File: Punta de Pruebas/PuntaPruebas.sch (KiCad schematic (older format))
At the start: 23 parts, among them P1 CONN_2, P2 CONN_1, P3 CONN_1, SW1 Llave Inversora, U1 40106

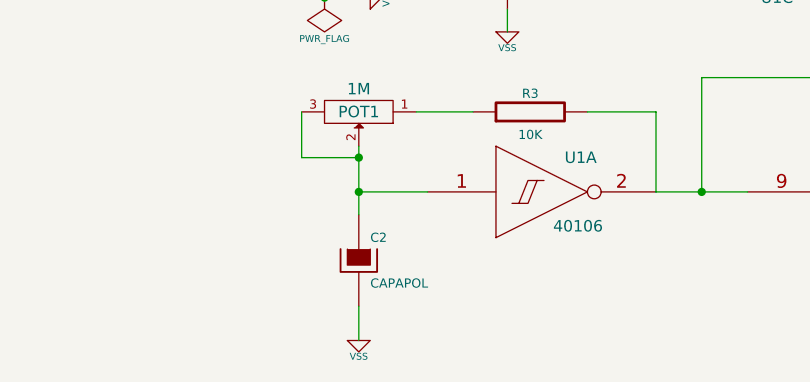
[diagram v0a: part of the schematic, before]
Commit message: Realizo un layout alternativo del PCB, haciendo más claro el ensamblado
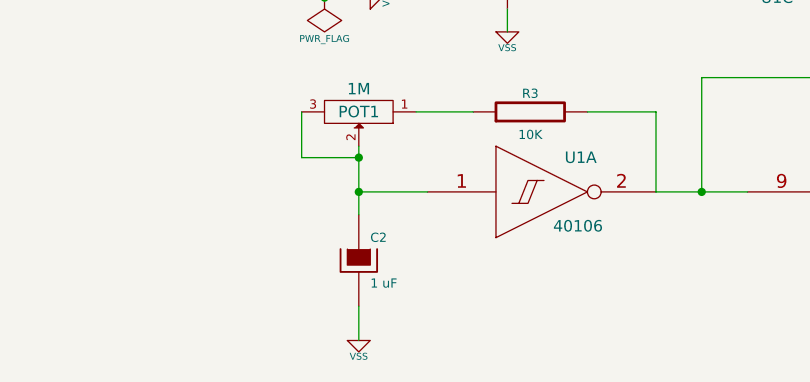
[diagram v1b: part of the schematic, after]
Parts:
- C2: value CAPAPOL -> 1 uF
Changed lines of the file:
@@
 LIBS:contrib
 LIBS:valves
-LIBS:w_device
 LIBS:PuntaPruebas-cache
-EELAYER 27 0
+EELAYER 24 0
 EELAYER END
 $Descr A4 11693 8268
@@
 Rev "1.0"
 Comp "Nestor A. Scoccia"
-Comment1 ""
+Comment1 "Proyecto N° 3"
 Comment2 ""
 Comment3 ""
@@
 P 3650 4950
 F 0 "C2" H 3700 5050 40  0000 L CNN
-F 1 "CAPAPOL" H 3700 4850 40  0000 L CNN
+F 1 "1 uF" H 3700 4850 40  0000 L CNN
 F 2 "~" H 3750 4800 30  0000 C CNN
 F 3 "~" H 3650 4950 300 0000 C CNN
